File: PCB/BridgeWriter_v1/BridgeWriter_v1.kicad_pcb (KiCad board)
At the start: 4 copper layers, 100 x 65 mm, 222 parts, among them J1 USB_B, J10 Barrel_Jack_MountingPin, J11 USB_C_Receptacle_PowerOnly_6P, J2 RJ45_Bel_SI-60062-F, J24 Conn_01x04, J25 Conn_01x04, J3 Conn_01x05, J4 Conn_01x06, J5 Conn_01x02, J6 Conn_01x04, J7 Conn_01x04, J8 Conn_01x02, J9 Micro_SD_Card_Det2, SW1 SW_Push, SW10 SW_Push, SW2 BOOT_MODE0, SW3 SW_Push, SW4 SW_Push, SW5 SW_Push, SW6 SW_Push, SW7 SW_Push, SW8 BOOT_MODE1, SW9 SW_Push, U1 STM32H723VGTx, U10 TPS1117LV33S, U11 OKL-T/6-W12N-C, U12 PT86-091940LMR, U13 AM8068, U14 AM8068, U15 MCP9700x-ETT, U16 MCP9700x-ETT, U18 USB_Type-C, U19 CH213K, U2 W6300, U20 KIA75S358F, U21 TLP293, U22 CH213K, U23 CH213K, U3 ESP32-C5-WROOM-1, U4 TLP293, U5 MCP2562-E-SN, U6 MCP2562-E-SN, U7 USB3343, U8 TPS1117LV33S, U9 CH221K, Y1 FC2012SN 32.768K-70NNA0KC0, Y2 XRCGB25M000FFS1AR0, Y3 ECS-600-8-36B-CTN-TR

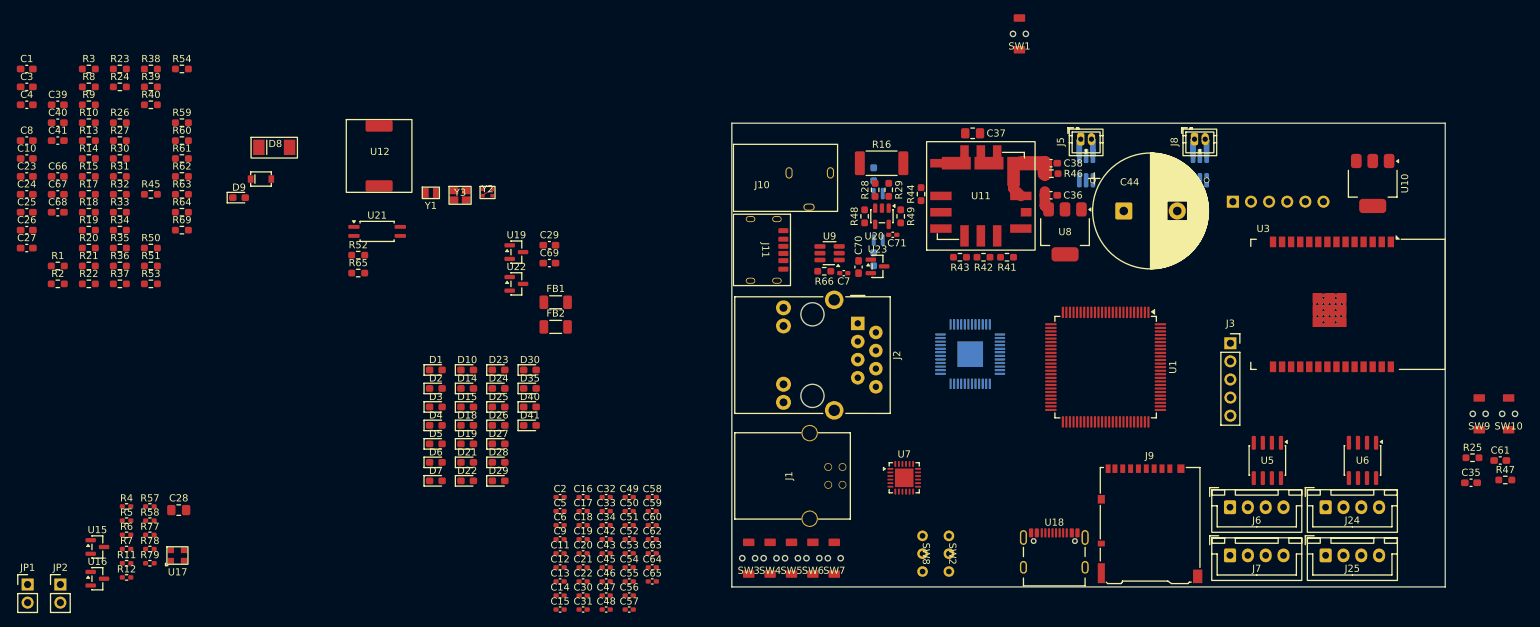
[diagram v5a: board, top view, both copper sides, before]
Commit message: PCB電源LED以外配線終わり　やること　LED追加と、シルクの被り解消
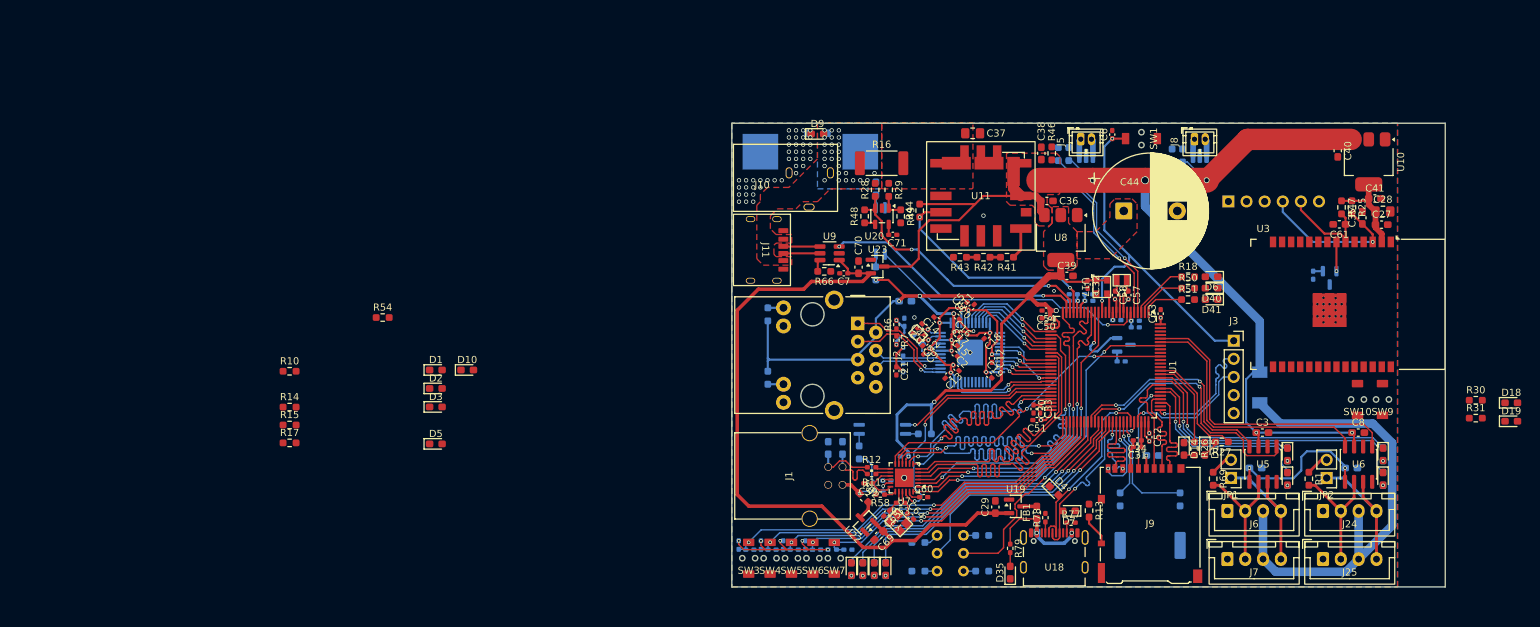
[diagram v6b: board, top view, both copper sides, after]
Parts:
- added C72: 0.1uF, Capacitor_SMD:C_0402_1005Metric_Pad0.74x0.62mm_HandSolder, B.Cu at (214.6, 93.4)
- added C73: 0.1uF, Capacitor_SMD:C_0402_1005Metric_Pad0.74x0.62mm_HandSolder, B.Cu at (241.5, 81.3)
- added J12: Conn_01x01, 0Ikedalibrary:5x5, B.Cu at (178.0, 64.0)
- added J13: Conn_01x01, 0Ikedalibrary:5x5, B.Cu at (164.0, 64.0)
- C1, C10, C22, C23, C24, C4, C45, C46, C47, C48, C49, C55, C56, C62, C63, D13, D27, D28, D8, R2, R23, R24, R3, R32, R33, R34, R35, R36, R37, R38, R39, R4, R40, R45, R5, R52, R57, R59, R60, R62, R63, R64, R65, R8, R9, U12, U15, U16, U21: moved to B.Cu
- C25, C26, C66, C67, C68: footprint Capacitor_SMD:C_0603_1608Metric_Pad1.08x0.95mm_HandSolder -> Capacitor_SMD:C_0402_1005Metric_Pad0.74x0.62mm_HandSolder; moved to B.Cu
- FB1, FB2: footprint Inductor_SMD:L_1206_3216Metric_Pad1.22x1.90mm_HandSolder -> Inductor_SMD:L_0603_1608Metric_Pad1.05x0.95mm_HandSolder
- R19, R20, R21, R22, R61: footprint Resistor_SMD:R_0603_1608Metric_Pad0.98x0.95mm_HandSolder -> Resistor_SMD:R_0402_1005Metric_Pad0.72x0.64mm_HandSolder; moved to B.Cu
- R53: footprint Resistor_SMD:R_0603_1608Metric_Pad0.98x0.95mm_HandSolder -> Resistor_SMD:R_0402_1005Metric_Pad0.72x0.64mm_HandSolder
- moved R30 193.1 mm to (264.3, 98.8)
- moved R31 193.1 mm to (264.3, 101.3)
- moved C8 191.1 mm to (247.8, 103.4)
- moved C10 190.7 mm to (246.8, 108.3), turned to 180 degrees
- moved C27 189.9 mm to (251.1, 74.2)
- moved C41 184.8 mm to (250.1, 70.5)
- moved R35 180.0 mm to (251.3, 109.8), turned to -90 degrees
- moved C3 179.9 mm to (234.4, 103.4)
- moved C4 179.6 mm to (233.4, 108.3), turned to 180 degrees
- moved C40 179.5 mm to (244.9, 63.9), turned to -90 degrees
- moved R36 179.0 mm to (251.3, 106.4), turned to -90 degrees
- moved JP2 178.1 mm to (243.4, 109.7), turned to 180 degrees
- moved R1 177.9 mm to (240.9, 109.8), turned to -90 degrees
- moved U15 176.8 mm to (243.8, 81.7), turned to -90 degrees
- moved C28 173.9 mm to (251.3, 72.4)
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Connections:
- FB2 pad 1: Net-(J1-VBUS) -> HS_VBUS
- J1 pad 1: Net-(J1-VBUS) -> HS_VBUS
- R52 pad 1: Net-(J1-VBUS) -> HS_VBUS
- R57 pad 2: VBUS -> HS_VBUS
- U1 pad 1: unconnected-(U1-PE2-Pad1) -> ERROR_LED
- U1 pad 16: unconnected-(U1-PC1-Pad16) -> Th_STM
- U1 pad 2: unconnected-(U1-PE3-Pad2) -> DEBUG_LED
- U1 pad 22: unconnected-(U1-PA0-Pad22) -> PGOOD
- U1 pad 23: unconnected-(U1-PA1-Pad23) -> POWER_ADC
- U1 pad 24: unconnected-(U1-PA2-Pad24) -> USB_PD_GOOD
- U1 pad 28: unconnected-(U1-PA4-Pad28) -> W6300_LNK
- U1 pad 3: unconnected-(U1-PE4-Pad3) -> WRITER_MODE
- U1 pad 30: unconnected-(U1-PA6-Pad30) -> W6300_SPD
- U1 pad 31: unconnected-(U1-PA7-Pad31) -> W6300_DPX
- U1 pad 32: unconnected-(U1-PC4-Pad32) -> W6300_ACT
- U1 pad 33: unconnected-(U1-PC5-Pad33) -> W6300_COL
- U1 pad 4: unconnected-(U1-PE5-Pad4) -> FAN_INB_STM
- U1 pad 42: unconnected-(U1-PE12-Pad42) -> W6300_INT
- U1 pad 43: unconnected-(U1-PE13-Pad43) -> W6300_RST
- U1 pad 44: unconnected-(U1-PE14-Pad44) -> USB_HS_CHECK
- U1 pad 45: unconnected-(U1-PE15-Pad45) -> USB3343_RESETB
- U1 pad 5: unconnected-(U1-PE6-Pad5) -> FAN_INA_STM
- U1 pad 53: unconnected-(U1-PB14-Pad53) -> FDCAN1_RESET
- U1 pad 54: unconnected-(U1-PB15-Pad54) -> FDCAN2_RESET
- U1 pad 55: unconnected-(U1-PD8-Pad55) -> Ethernet_RESET
- U1 pad 56: unconnected-(U1-PD9-Pad56) -> USB_RESET
- U1 pad 57: unconnected-(U1-PD10-Pad57) -> Wi-Fi_RESET
- U1 pad 58: unconnected-(U1-PD11-Pad58) -> USB_TX
- U1 pad 61: unconnected-(U1-PD14-Pad61) -> USB_RX
- U1 pad 62: unconnected-(U1-PD15-Pad62) -> Ethernet_TX
- U1 pad 63: unconnected-(U1-PC6-Pad63) -> Ethernet_RX
- U1 pad 64: unconnected-(U1-PC7-Pad64) -> BOOTMODE
- U1 pad 67: unconnected-(U1-PA8-Pad67) -> SDMMC_CHECK
- U1 pad 68: unconnected-(U1-PA9-Pad68) -> Speaker_In1
- U1 pad 69: unconnected-(U1-PA10-Pad69) -> Speaker_In2
- U1 pad 7: unconnected-(U1-PC13-Pad7) -> POWER_MONITOR
- U1 pad 81: unconnected-(U1-PD0-Pad81) -> FDCAN2_TX
- U1 pad 82: unconnected-(U1-PD1-Pad82) -> FDCAN2_RX
- U1 pad 84: unconnected-(U1-PD3-Pad84) -> FDCAN1_TX
- U1 pad 85: unconnected-(U1-PD4-Pad85) -> FDCAN1_RX
- U1 pad 86: unconnected-(U1-PD5-Pad86) -> SDMMC_WRITE
- U1 pad 87: unconnected-(U1-PD6-Pad87) -> SDMMC_READ
- U15 pad 1: +5V -> ESP_3.3V
- U16 pad 1: +5V -> +3.3V
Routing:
- net +3.3V: track 0.00 -> 257.2 mm, vias 0 -> 28
- net +5V: track 11.4 -> 151.3 mm, vias 2 -> 6
- net VBUS: track 0.00 -> 99.0 mm
- net W6300_LNK: track 0.00 -> 68.0 mm, vias 0 -> 1
- net +5VA: track 0.00 -> 67.5 mm
- net FDCAN1_RESET: track 0.00 -> 55.4 mm, vias 0 -> 2
- net FDCAN2_RESET: track 0.00 -> 52.9 mm, vias 0 -> 2
- net Ethernet_RESET: track 0.00 -> 50.4 mm, vias 0 -> 2
- net W6300_ACT: track 0.00 -> 50.2 mm, vias 0 -> 1
- net NRST: track 0.00 -> 50.1 mm, vias 0 -> 2
- net USB_OTG_HS_ULPI_D1: track 0.00 -> 48.0 mm
- net STM32_BOOT0: track 0.00 -> 47.9 mm, vias 0 -> 2
- net USB_OTG_HS_ULPI_D2: track 0.00 -> 47.9 mm
- net USB_RESET: track 0.00 -> 47.9 mm, vias 0 -> 2
- net Wi-Fi_RESET: track 0.00 -> 45.6 mm, vias 0 -> 2
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- added copper zone on F.Cu, net +3.3V
- added copper zone on F.Cu, net +5V
- added copper zone on B.Cu, net GND
- added copper zone on F.Cu, net GND
- added copper zone on In1.Cu, net GND
- added copper zone on In2.Cu, net GND
- added copper zone on B.Cu, net VCC
- added copper zone on F.Cu, net VCC
- added copper zone on F.Cu, net VCC_IO

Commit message: ほぼ完成
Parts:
- R15, R17: moved to B.Cu
- moved R54 124.2 mm to (234.6, 74.6)
- moved D10 116.7 mm to (237.9, 74.6), turned to 180 degrees
- moved R17 113.8 mm to (203.3, 61.6)
- moved R15 109.8 mm to (200.0, 61.6)
- moved D5 95.2 mm to (203.3, 61.6)
- moved D2 88.9 mm to (200.0, 61.6)
- moved R10 80.5 mm to (176.1, 75.3), turned to 180 degrees
- moved R14 80.0 mm to (168.2, 61.5), turned to 180 degrees
- moved D3 59.6 mm to (172.8, 75.3)
- moved D1 57.0 mm to (164.9, 61.5)
- moved D19 25.9 mm to (243.5, 99.0), turned to 180 degrees
- moved D18 25.8 mm to (243.5, 97.5), turned to 180 degrees
- moved R31 24.1 mm to (240.2, 99.0)
- moved R30 24.1 mm to (240.2, 97.5)
- moved C33 0.23 mm to (203.0, 99.9)
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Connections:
- U1 pad 86: SDMMC_WRITE -> FW_UART_TX
- U1 pad 87: SDMMC_READ -> FW_UART_RX
- U1 pad 92: unconnected-(U1-PB6-Pad92) -> SDMMC_WRITE
- U1 pad 93: unconnected-(U1-PB7-Pad93) -> SDMMC_READ
- U1 pad 97: unconnected-(U1-PE0-Pad97) -> FW_UART_TXF
- U1 pad 98: unconnected-(U1-PE1-Pad98) -> FW_UART_RXF
- U3 pad 13: Wi-Fi_RX -> FAN_INB_ESP
- U3 pad 14: Wi-Fi_TX -> FAN_INA_ESP
- U3 pad 15: FAN_INB_ESP -> FW_UART_TXF
- U3 pad 16: FW_UART_RX -> FW_UART_TX
- U3 pad 17: FW_UART_TX -> FW_UART_RX
- U3 pad 18: FAN_INA_ESP -> FW_UART_RXF
- U3 pad 19: FW_UART_RXF -> Wi-Fi_RX
- U3 pad 21: FW_UART_TXF -> Wi-Fi_TX
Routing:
- net +3.3V: track 257.2 -> 368.5 mm, vias 28 -> 32
- net +5V: track 151.3 -> 231.7 mm, vias 6 -> 8
- net ESP_3.3V: track 14.2 -> 60.3 mm, vias 0 -> 1
- net TXD0: track 0.00 -> 32.8 mm, vias 0 -> 1
- net RXD0: track 0.00 -> 30.0 mm, vias 0 -> 1
- net FW_UART_RXF: track 0.00 -> 25.1 mm
- net FW_UART_RX: track 0.00 -> 24.2 mm, vias 0 -> 2
- net FW_UART_TX: track 0.00 -> 23.2 mm, vias 0 -> 2
- net FW_UART_TXF: track 0.00 -> 21.8 mm, vias 0 -> 2
- net ESP32_IO0: track 13.7 -> 34.5 mm, vias 0 -> 2
- net ESP32_EN: track 21.0 -> 41.4 mm, vias 1 -> 2
- net GND: track 11.8 -> 28.9 mm, vias 52 -> 459
- net FAN_INB_ESP: track 3.96 -> 20.4 mm, vias 0 -> 1
- net FAN_INA_ESP: track 4.00 -> 19.7 mm, vias 0 -> 1
- net VBUS: track 99.0 -> 105.5 mm
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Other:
- board text added: "3.3V"
- board text added: "5V"
- board text added: "BOOT0"
- board text added: "BOOTM"
- board text added: "DEBUG"
- board text added: "Dis"
- board text added: "ERROR"
- board text added: "ESP_3.3V"
- board text added: "Ena"
- board text added: "Ethernet"
- board text added: "FDCAN1"
- board text added: "FDCAN2"
- board text added: "MicroSD"
- board text added: "READ"
- board text added: "RX"
- board text added: "SYS"
- board text added: "TX"
- board text added: "USB"
- board text added: "USB_DFU"
- board text added: "USER"
- board text added: "VBUS"
- board text added: "VCC"
- board text added: "WRITE"
- board text added: "Wi-Fi"

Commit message: PCB一応完成
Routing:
- net GND: vias 459 -> 468
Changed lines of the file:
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@@
 	)
 	(via
-		(at 238 98)
-		(size 0.5)
-		(drill 0.3)
-		(layers "F.Cu" "B.Cu")
-		(free yes)
-		(net 1)
-	)
-	(via
 		(at 252 78)
 		(size 0.5)
@@
 	)
 	(via
+		(at 208.5 70.3)
+		(size 0.6)
+		(drill 0.4)
+		(layers "F.Cu" "B.Cu")
+		(free yes)
+		(net 1)
+	)
+	(via
 		(at 252 79)
 		(size 0.5)
@@
 	)
 	(via
+		(at 234 97.5)
+		(size 0.5)
+		(drill 0.3)
+		(layers "F.Cu" "B.Cu")
+		(free yes)
+		(net 1)
+	)
+	(via
 		(at 239 100)
 		(size 0.5)
@@
 	)
 	(via
+		(at 207 71)
+		(size 0.6)
+		(drill 0.4)
+		(layers "F.Cu" "B.Cu")
+		(free yes)
+		(net 1)
+	)
+	(via
+		(at 208 71)
+		(size 0.6)
+		(drill 0.4)
+		(layers "F.Cu" "B.Cu")
+		(free yes)
+		(net 1)
+	)
+	(via
 		(at 224 76)
 		(size 0.5)
@@
 	)
 	(via
+		(at 210 73)
+		(size 0.6)
+		(drill 0.4)
+		(layers "F.Cu" "B.Cu")
+		(free yes)
+		(net 1)
+	)
+	(via
 		(at 226 78)
 		(size 0.5)
@@
 	)
 	(via
-		(at 238 97)
-		(size 0.5)
-		(drill 0.3)
-		(layers "F.Cu" "B.Cu")
-		(free yes)
-		(net 1)
-	)
-	(via
 		(at 188 97)
 		(size 0.5)
@@
 	)
 	(via
-		(at 235 98)
-		(size 0.5)
-		(drill 0.3)
-		(layers "F.Cu" "B.Cu")
-		(free yes)
-		(net 1)
-	)
-	(via
 		(at 252 71)
 		(size 0.5)
@@
 	)
 	(via
-		(at 234 97)
+		(at 234 96.5)
 		(size 0.5)
 		(drill 0.3)
@@
 	)
 	(via
-		(at 233 97)
+		(at 233 96.5)
 		(size 0.5)
 		(drill 0.3)
@@
 	)
 	(via
+		(at 209 71)
+		(size 0.6)
+		(drill 0.4)
+		(layers "F.Cu" "B.Cu")
+		(free yes)
+		(net 1)
+	)
+	(via
 		(at 171 64)
 		(size 0.6)
@@
 	)
 	(via
-		(at 233 98)
-		(size 0.5)
-		(drill 0.3)
-		(layers "F.Cu" "B.Cu")
-		(free yes)
-		(net 1)
-	)
-	(via
 		(at 170 81)
 		(size 0.5)
@@
 	)
 	(via
-		(at 192 70)
+		(at 233 97.5)
 		(size 0.5)
 		(drill 0.3)
@@
 	)
 	(via
-		(at 208 122)
+		(at 192 70)
 		(size 0.5)
 		(drill 0.3)
@@
 	)
 	(via
-		(at 222 74)
+		(at 208 122)
 		(size 0.5)
 		(drill 0.3)
@@
 	)
 	(via
-		(at 234 98)
+		(at 222 74)
 		(size 0.5)
 		(drill 0.3)
@@
 	)
 	(via
-		(at 235 97)
+		(at 235 96.5)
 		(size 0.5)
 		(drill 0.3)
@@
 	)
 	(via
+		(at 211.5 70.5)
+		(size 0.6)
+		(drill 0.4)
+		(layers "F.Cu" "B.Cu")
+		(free yes)
+		(net 1)
+	)
+	(via
 		(at 222 61)
 		(size 0.6)
@@
 	)
 	(via
+		(at 209.7 71.3)
+		(size 0.6)
+		(drill 0.4)
+		(layers "F.Cu" "B.Cu")
+		(free yes)
+		(net 1)
+	)
+	(via
 		(at 197 69)
 		(size 0.5)
@@
 	)
 	(via
+		(at 210 74)
+		(size 0.6)
+		(drill 0.4)
+		(layers "F.Cu" "B.Cu")
+		(free yes)
+		(net 1)
+	)
+	(via
 		(at 196 62)
 		(size 0.5)
@@
 	)
 	(via
+		(at 209 74.5)
+		(size 0.6)
+		(drill 0.4)
+		(layers "F.Cu" "B.Cu")
+		(free yes)
+		(net 1)
+	)
+	(via
 		(at 252 67)
 		(size 0.5)
@@
 	)
 	(via
+		(at 207.5 70.3)
+		(size 0.6)
+		(drill 0.4)
+		(layers "F.Cu" "B.Cu")
+		(free yes)
+		(net 1)
+	)
+	(via
 		(at 212 90)
 		(size 0.5)
@@
 	)
 	(via
-		(at 211.13 83.88)
-		(size 0.5)
-		(drill 0.3)
+		(at 206.5 70.3)
+		(size 0.6)
+		(drill 0.4)
 		(layers "F.Cu" "B.Cu")
+		(free yes)
 		(net 1)
 	)
 	(via
-		(at 170 74)
+		(at 211.13 83.88)
 		(size 0.5)
 		(drill 0.3)
 		(layers "F.Cu" "B.Cu")
-		(free yes)
 		(net 1)
 	)
 	(via
-		(at 161 81)
+		(at 170 74)
 		(size 0.5)
 		(drill 0.3)
@@
 	)
 	(via
-		(at 233 96)
+		(at 161 81)
 		(size 0.5)
 		(drill 0.3)
@@
 	)
 	(via
-		(at 234 96)
-		(size 0.5)
-		(drill 0.3)
-		(layers "F.Cu" "B.Cu")
-		(free yes)
-		(net 1)
-	)
-	(via
 		(at 221 61)
 		(size 0.6)
@@
 	)
 	(via
-		(at 235 96)
-		(size 0.5)
-		(drill 0.3)
-		(layers "F.Cu" "B.Cu")
-		(free yes)
-		(net 1)
-	)
-	(via
 		(at 174 74)
 		(size 0.5)
@@
 	)
 	(via
+		(at 235 97.5)
+		(size 0.5)
+		(drill 0.3)
+		(layers "F.Cu" "B.Cu")
+		(free yes)
+		(net 1)
+	)
+	(via
 		(at 186 97)
 		(size 0.5)
@@
 	)
 	(via
+		(at 213 70.5)
+		(size 0.6)
+		(drill 0.4)
+		(layers "F.Cu" "B.Cu")
+		(free yes)
+		(net 1)
+	)
+	(via
 		(at 198 73)
 		(size 0.5)
@@
 	)
 	(via
+		(at 206 71)
+		(size 0.6)
+		(drill 0.4)
+		(layers "F.Cu" "B.Cu")
+		(free yes)
+		(net 1)
+	)
+	(via
+		(at 210 72)
+		(size 0.6)
+		(drill 0.4)
+		(layers "F.Cu" "B.Cu")
+		(free yes)
+		(net 1)
+	)
+	(via
 		(at 203.38 63.367499)
 		(size 0.5)
@@
 	)
 	(segment
-		(start 209.66 67.290011)
-		(end 209.66 68.000002)
+		(start 211.001 74.852464)
+		(end 211.001 71.041)
 		(width 0.2)
 		(layer "B.Cu")
@@
 	)
 	(segment
-		(start 211.13 71.17)
-		(end 209.66 69.7)
+		(start 209.66 67.290011)
+		(end 209.66 68.000002)
 		(width 0.2)
 		(layer "B.Cu")
@@
 	)
 	(segment
-		(start 215.074268 78.925732)
-		(end 211.13 74.981464)
+		(start 211.001 71.041)
+		(end 209.66 69.7)
 		(width 0.2)
 		(layer "B.Cu")
@@
 	)
 	(segment
-		(start 211.13 74.981464)
-		(end 211.13 71.17)
+		(start 215.074268 78.925732)
+		(end 211.001 74.852464)
 		(width 0.2)
 		(layer "B.Cu")
@@
 	)
 	(segment
-		(start 208.520001 68.000001)
-		(end 205.76 65.24)
+		(start 208.71 69.3171)
+		(end 208.71 68.000001)
 		(width 0.2)
 		(layer "B.Cu")
@@
 	)
 	(segment
-		(start 210.729 71.3361)
-		(end 208.71 69.3171)
+		(start 214.305359 78.934641)
+		(end 210.6 75.229282)
 		(width 0.2)
 		(layer "B.Cu")
@@
 	)
 	(segment
-		(start 210.729 75.358282)
-		(end 210.729 71.3361)
+		(start 208.520001 68.000001)
+		(end 205.76 65.24)
 		(width 0.2)
 		(layer "B.Cu")
@@
 	)
 	(segment
-		(start 208.71 69.3171)
-		(end 208.71 68.000001)
+		(start 210.6 75.229282)
+		(end 210.6 71.2071)
 		(width 0.2)
 		(layer "B.Cu")
@@
 	)
 	(segment
-		(start 214.305359 78.934641)
-		(end 210.729 75.358282)
+		(start 210.6 71.2071)
+		(end 208.71 69.3171)
 		(width 0.2)
 		(layer "B.Cu")
